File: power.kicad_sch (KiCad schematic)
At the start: 18 parts, among them J10 CX90B1-24P, J11 HTSW-102-07-G-S, J2 HTSW-102-07-G-S, J9 HTSW-102-07-G-S, U1 TPSM861253RDXR

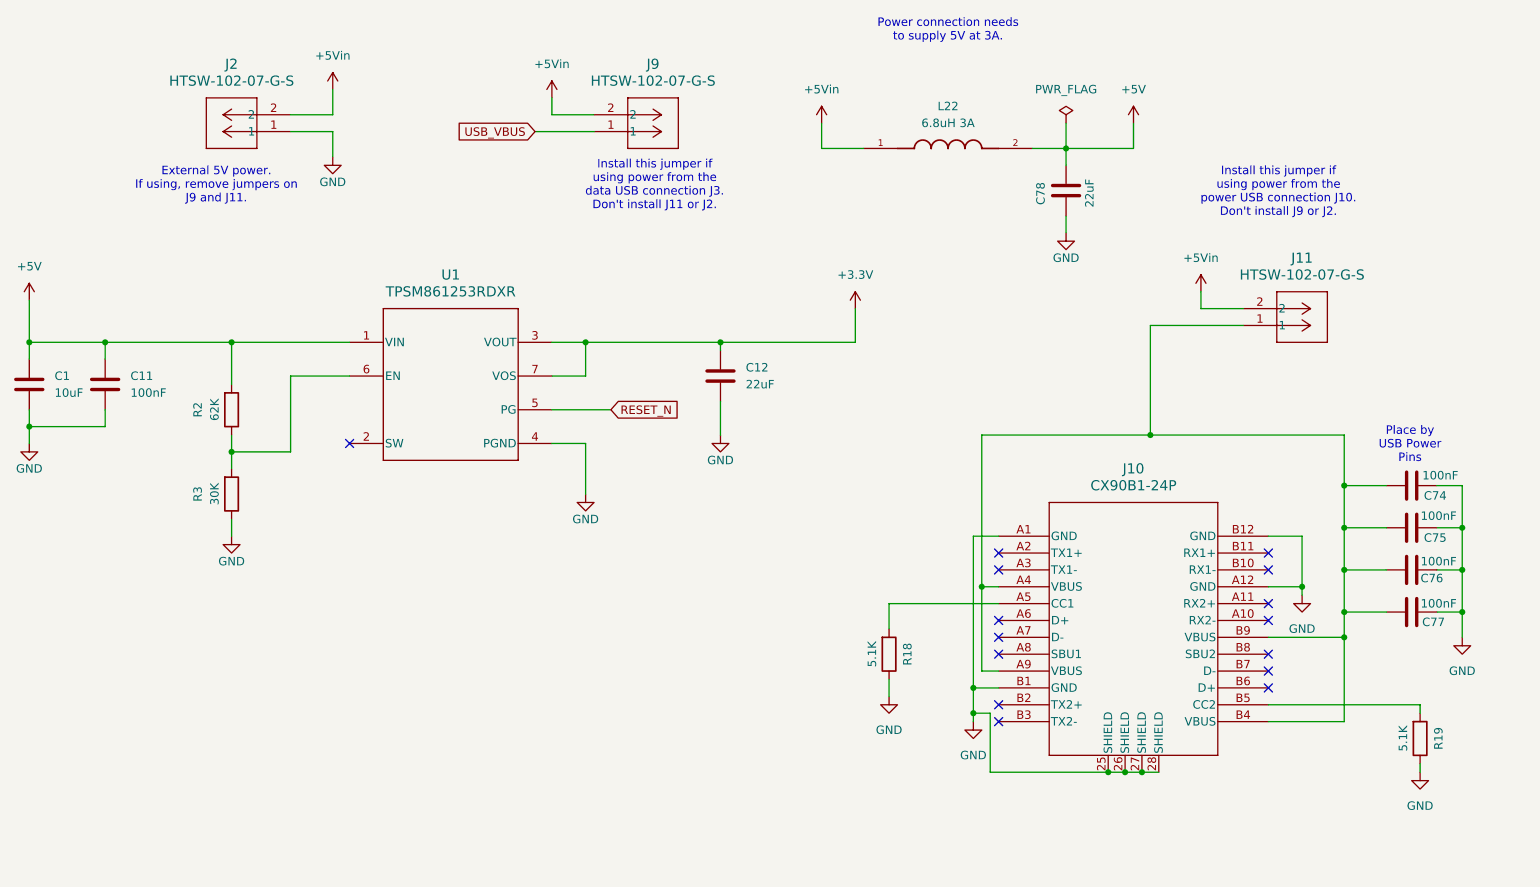
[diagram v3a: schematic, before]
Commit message: Add pull up on the PA enables
So they are off by default.

Signed-off-by: Corey Minyard <corey@minyard.net>
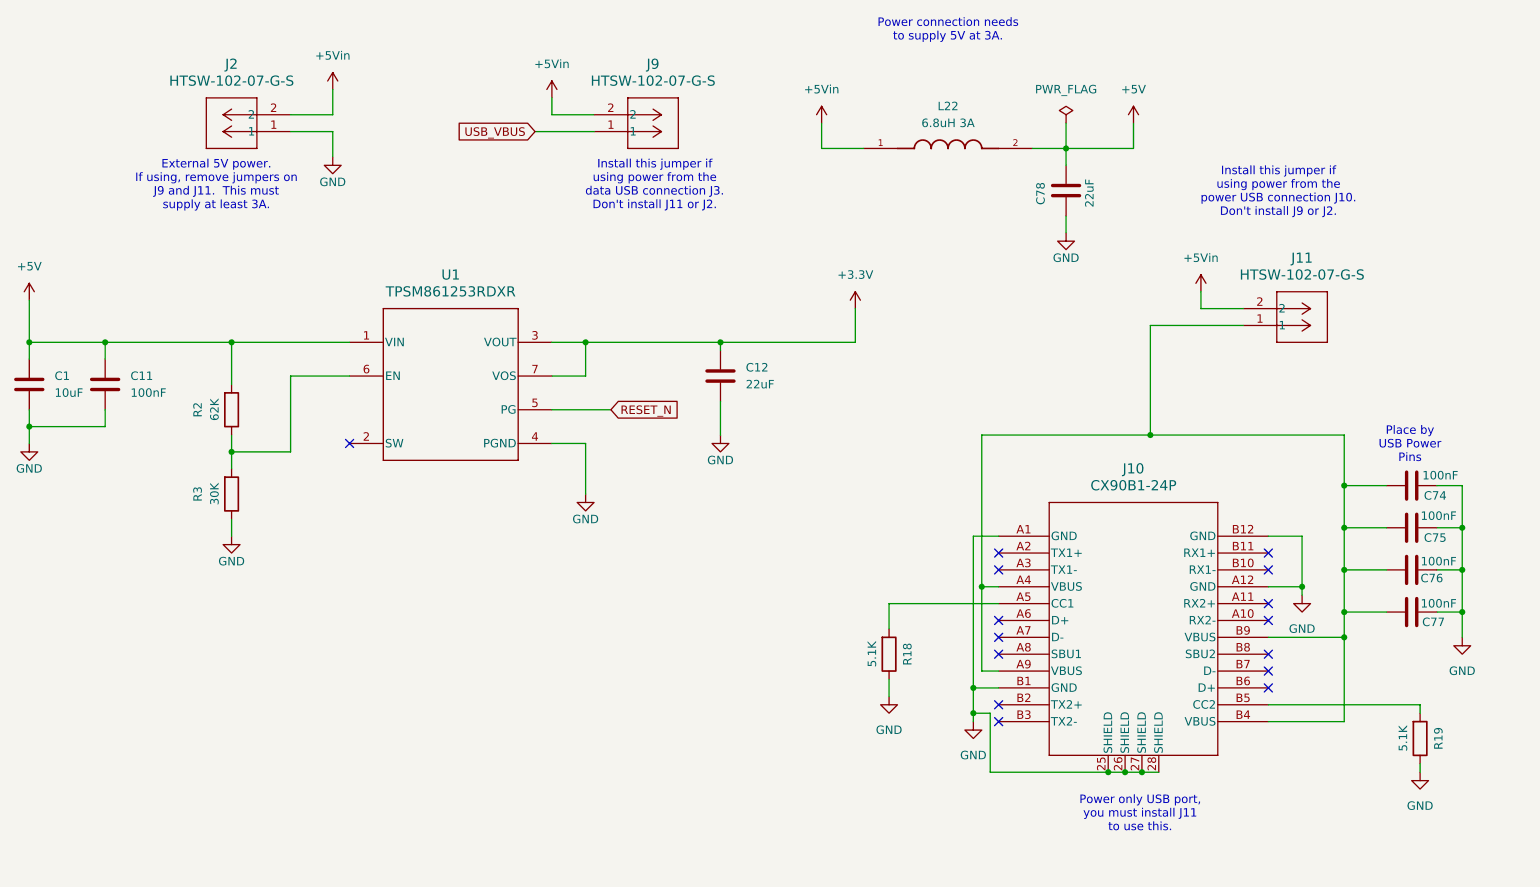
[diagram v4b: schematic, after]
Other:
- note added: "External 5V power. If using, remove jumpers on J9 and J11. This must supply at least 3A."
- note added: "Power only USB port, you must install J11 to use this."
- note removed: "External 5V power. If using, remove jumpers on J9 and J11."
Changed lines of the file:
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@@
+		)
+	)
+	(text "Power only USB port,\nyou must install J11\nto use this."
+		(exclude_from_sim no)
+		(at 201.676 138.43 0)
+		(effects
+			(font
+				(size 1.27 1.27)
+			)
 		)
 	)
@@
 		)
 	)
-	(text "External 5V power.\nIf using, remove jumpers on\nJ9 and J11."
+	(text "External 5V power.\nIf using, remove jumpers on\nJ9 and J11.  This must\nsupply at least 3A."
 		(exclude_from_sim no)
 		(at 62.484 43.688 0)

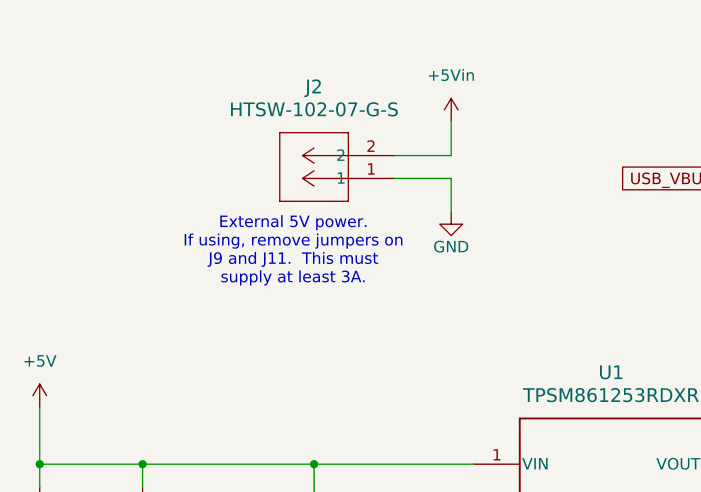
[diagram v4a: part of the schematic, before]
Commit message: Add a barrel-type power connector
Make supplying power a little simpler.

Signed-off-by: Corey Minyard <corey@minyard.net>
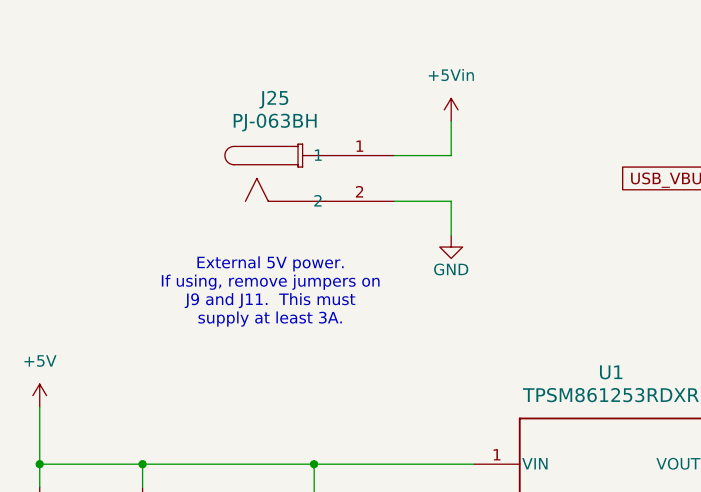
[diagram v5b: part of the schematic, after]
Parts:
- removed J2: HTSW-102-07-G-S, footprints:CON2_1X2_TU_TSW, symbol Local Connectors:HTSW-102-07-G-S
- added J25: PJ-063BH, footprints:PJ-063BH_CUD, symbol Local Connectors:PJ-063BH
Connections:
- net +5Vin: now also J25.1
- net GND: now also J25.2
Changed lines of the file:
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@@
 	(text "External 5V power.\nIf using, remove jumpers on\nJ9 and J11.  This must\nsupply at least 3A."
 		(exclude_from_sim no)
-		(at 62.484 43.688 0)
+		(at 59.944 48.26 0)
 		(effects
 			(font
@@
 	(wire
 		(pts
-			(xy 80.01 35.56) (xy 80.01 39.37)
+			(xy 80.01 38.1) (xy 80.01 41.91)
 		)
 		(stroke
@@
 	(wire
 		(pts
-			(xy 73.66 35.56) (xy 80.01 35.56)
+			(xy 73.66 38.1) (xy 80.01 38.1)
 		)
 		(stroke
@@
 	)
 	(symbol
+		(lib_id "Local Connectors:PJ-063BH")
+		(at 73.66 33.02 0)
+		(unit 1)
+		(exclude_from_sim no)
+		(in_bom yes)
+		(on_board yes)
+		(dnp no)
+		(fields_autoplaced yes)
+		(property "Reference" "J25"
+			(at 60.4542 26.67 0)
+			(effects
+				(font
+					(size 1.524 1.524)
+				)
+			)
+		)
+		(property "Value" "PJ-063BH"
+			(at 60.4542 29.21 0)
+			(effects
+				(font
+					(size 1.524 1.524)
+				)
+			)
+		)
+		(property "Footprint" "footprints:PJ-063BH_CUD"
+			(at 78.74 25.908 0)
+			(effects
+				(font
+					(size 1.27 1.27)
+					(italic yes)
+				)
+				(hide yes)
+			)
+		)
+		(property "Datasheet" "PJ-063BH"
+			(at 77.216 28.448 0)
+			(effects
+				(font
+					(size 1.27 1.27)
+					(italic yes)
+				)
+				(hide yes)
+			)
+		)
+		(property "Description" ""
+			(at 73.66 33.02 0)
+			(effects
+				(font
+					(size 1.27 1.27)
+				)
+				(hide yes)
+			)
+		)
+		(pin "1"
+		)
+		(pin "2"
+		)
+		(instances
+			(project ""
+				(path "/23e49ab9-97e0-460a-806c-ff6f37958474/7a6bdc95-f709-4212-bcb6-cbe36d3e80bf"
+					(reference "J25")
+					(unit 1)
+				)
+			)
+		)
+	)
+	(symbol
 		(lib_id "Device:C")
 		(at 190.5 44.45 180)
@@
 	(symbol
 		(lib_id "power:GND")
-		(at 80.01 39.37 0)
+		(at 80.01 41.91 0)
 		(unit 1)
 		(exclude_from_sim no)
@@
 		(dnp no)
 		(property "Reference" "#PWR012"
-			(at 80.01 45.72 0)
+			(at 80.01 48.26 0)
 			(effects
 				(font
@@
 		)
 		(property "Value" "GND"
-			(at 80.01 43.18 0)
+			(at 80.01 45.72 0)
 			(effects
 				(font
@@
 		)
 		(property "Footprint" ""
-			(at 80.01 39.37 0)
+			(at 80.01 41.91 0)
 			(effects
 				(font
@@
 		)
 		(property "Datasheet" ""
-			(at 80.01 39.37 0)
+			(at 80.01 41.91 0)
 			(effects
 				(font
@@
 		)
 		(property "Description" "Power symbol creates a global label with name \"GND\" , ground"
-			(at 80.01 39.37 0)
+			(at 80.01 41.91 0)
 			(effects
 				(font
@@
 					(unit 1)
 				)
-			)
-		)
-	)
-	(symbol
-		(lib_id "Local Connectors:HTSW-102-07-G-S")
-		(at 73.66 35.56 180)
-		(unit 1)
-		(exclude_from_sim no)
-		(in_bom yes)
-		(on_board yes)
-		(dnp no)
-		(fields_autoplaced yes)
-		(property "Reference" "J2"
-			(at 64.77 25.4 0)
-			(effects
-				(font
-					(size 1.524 1.524)
-				)
-			)
-		)
-		(property "Value" "HTSW-102-07-G-S"
-			(at 64.77 27.94 0)
-			(effects
-				(font
-					(size 1.524 1.524)
-				)
-			)
-		)
-		(property "Footprint" "footprints:CON2_1X2_TU_TSW"
-			(at 73.66 35.56 0)
-			(effects
-				(font
-					(size 1.27 1.27)
-					(italic yes)
-				)
-				(hide yes)
-			)
-		)
-		(property "Datasheet" "HTSW-102-07-G-S"
-			(at 73.66 35.56 0)
-			(effects
-				(font
-					(size 1.27 1.27)
-					(italic yes)
-				)
-				(hide yes)
-			)
-		)
-		(property "Description" ""
-			(at 73.66 35.56 0)
-			(effects
-				(font
-					(size 1.27 1.27)
-				)
-				(hide yes)
-			)
-		)
-		(pin "2"
-		)
-		(pin "1"
-		)
-		(instances
-			(project ""
-				(path "/23e49ab9-97e0-460a-806c-ff6f37958474/7a6bdc95-f709-4212-bcb6-cbe36d3e80bf"
-					(reference "J2")
-					(unit 1)
-				)

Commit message: Missed the schematic save on the new LED
Signed-off-by: Corey Minyard <corey@minyard.net>
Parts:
- added D2: BLUE LED, LED_SMD:LED_0603_1608Metric_Pad1.05x0.95mm_HandSolder, symbol Device:LED
- added R43: 2.4KΩ, Resistor_SMD:R_0603_1608Metric_Pad0.98x0.95mm_HandSolder, symbol Device:R
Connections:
- net +5V: now also D2.2 (A)
- net GND: now also R43.2
- new net: D2.1 (K), R43.1

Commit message: Split the USB CPU and main CPU reset lines
Signed-off-by: Corey Minyard <corey@minyard.net>
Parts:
- added C13: 100nF, Capacitor_SMD:C_0402_1005Metric_Pad0.74x0.62mm_HandSolder, symbol Device:C
- added R44: 10K, Resistor_SMD:R_0402_1005Metric, symbol Device:R
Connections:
- net +3.3V: now also R44.2
- net GND: now also C13.1
- net RESET_N: now also C13.2, R44.1
